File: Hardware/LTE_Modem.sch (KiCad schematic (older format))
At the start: 23 parts, among them J1 Bus_PCI_Express_Mini, J2 SIM_Card

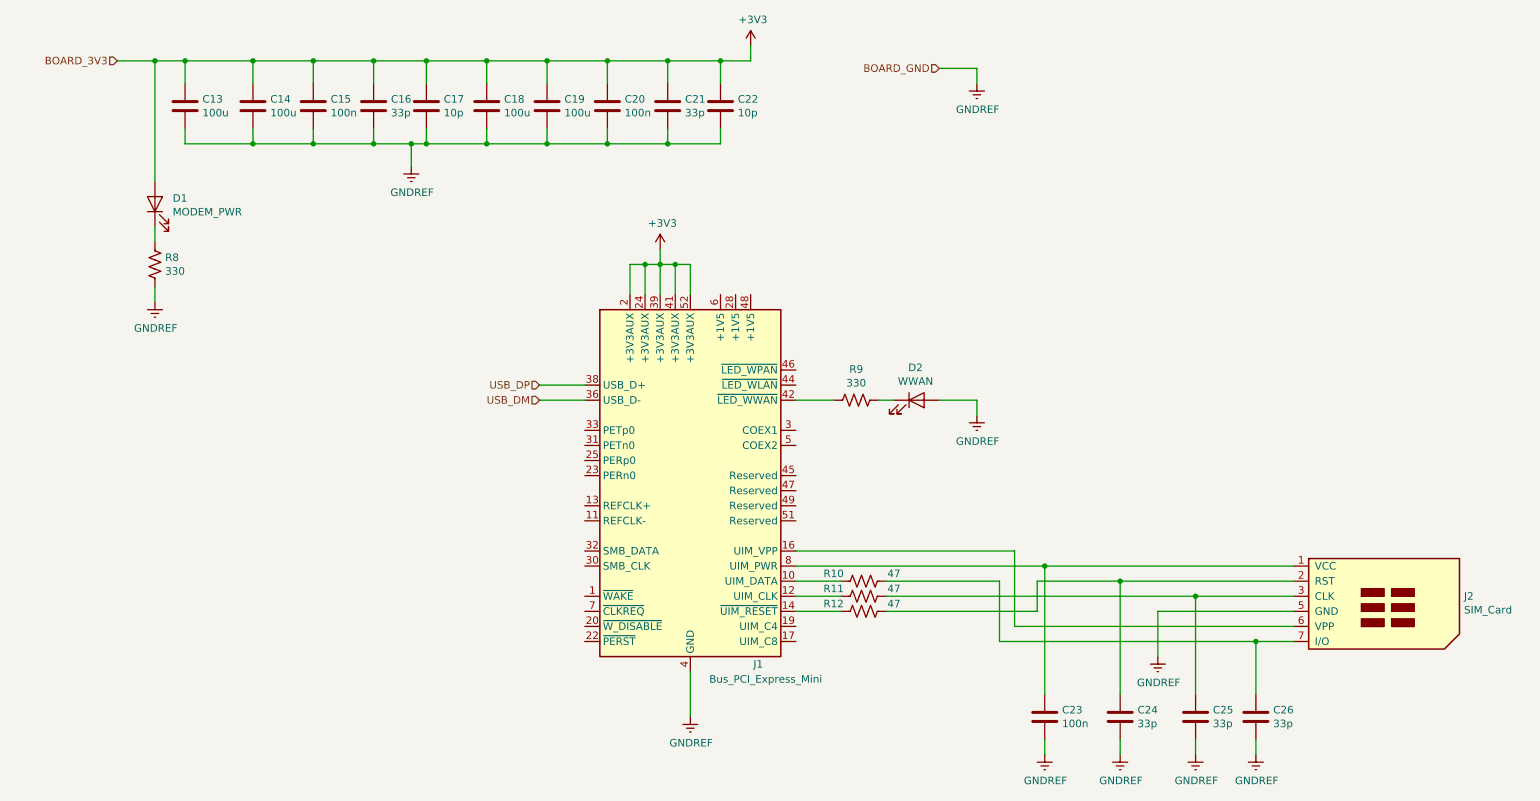
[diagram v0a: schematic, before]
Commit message: Added footprints to schematic symbols
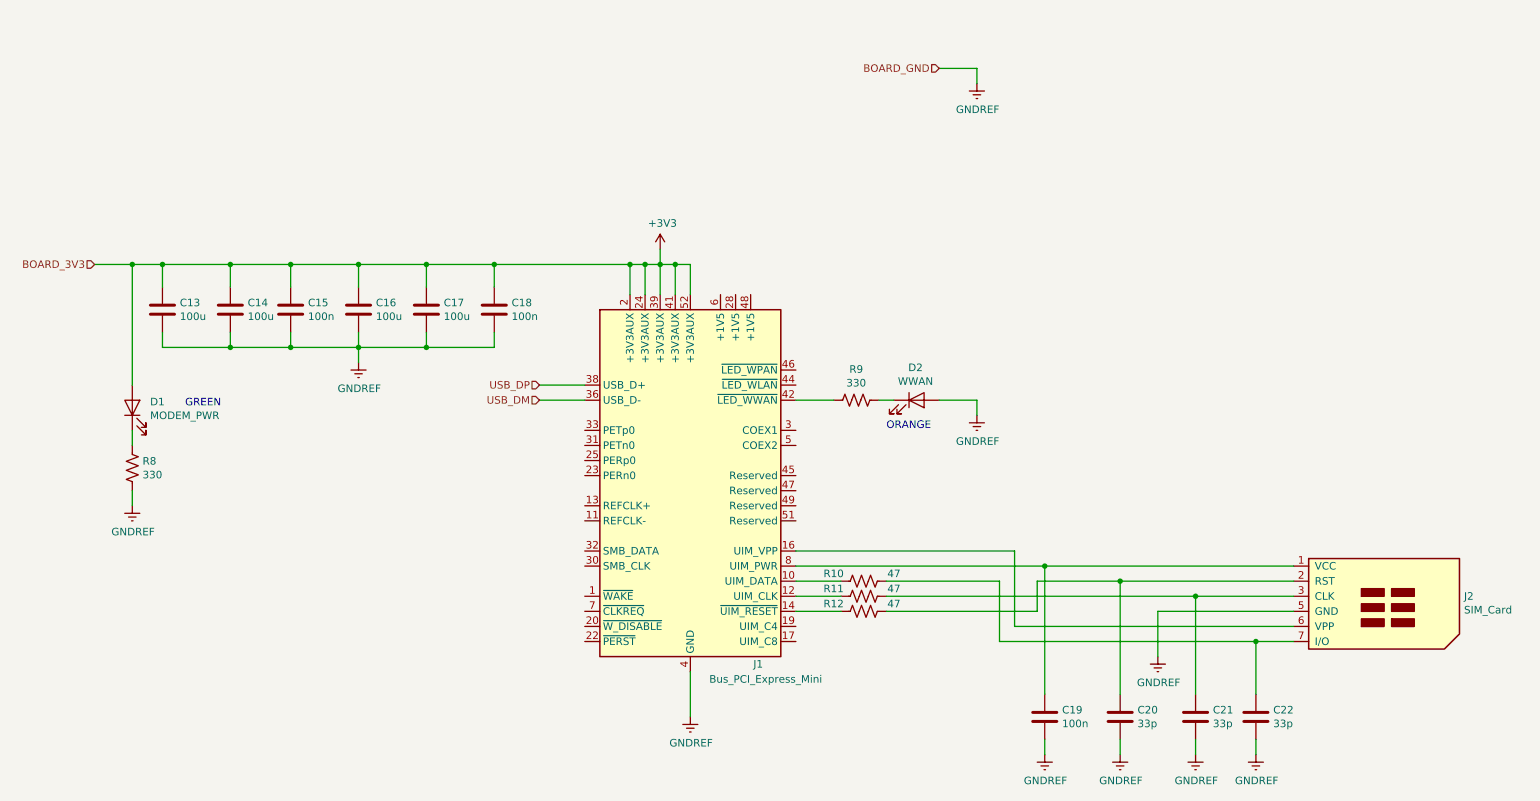
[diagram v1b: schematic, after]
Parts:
- removed C16, C21: 33p, symbol Device:C
- removed C17, C22: 10p, symbol Device:C
- C13, C14: footprint (none) -> Capacitor_SMD:C_1206_3216Metric_Pad1.42x1.75mm_HandSolder
- C15: footprint (none) -> Capacitor_SMD:C_0603_1608Metric_Pad1.05x0.95mm_HandSolder
- C16: renamed from C18; footprint (none) -> Capacitor_SMD:C_1206_3216Metric_Pad1.42x1.75mm_HandSolder
- C17: renamed from C19; footprint (none) -> Capacitor_SMD:C_1206_3216Metric_Pad1.42x1.75mm_HandSolder
- C18: renamed from C20; footprint (none) -> Capacitor_SMD:C_0603_1608Metric_Pad1.05x0.95mm_HandSolder
- C19: renamed from C23; footprint (none) -> Capacitor_SMD:C_0603_1608Metric_Pad1.05x0.95mm_HandSolder
- C20: renamed from C24; footprint (none) -> Capacitor_SMD:C_0603_1608Metric_Pad1.05x0.95mm_HandSolder
- C21: renamed from C25; footprint (none) -> Capacitor_SMD:C_0603_1608Metric_Pad1.05x0.95mm_HandSolder
- C22: renamed from C26; footprint (none) -> Capacitor_SMD:C_0603_1608Metric_Pad1.05x0.95mm_HandSolder
- D1, D2: footprint (none) -> LED_SMD:LED_0805_2012Metric_Castellated
- J1: footprint (none) -> MiniPCIe:mpcie-socket
- J2: footprint (none) -> SIM:SIM_115C_AC00_R
- R10, R11, R12, R8, R9: footprint (none) -> Resistor_SMD:R_1206_3216Metric
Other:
- note added: "GREEN"
- note added: "ORANGE"
- moved on the sheet: C13, C14, C15, C16, C17, C18, D1, R8
